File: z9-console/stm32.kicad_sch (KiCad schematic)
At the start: 73 parts, among them J4 Conn_02x20_Odd_Even, J5 ST_STDC14 - SAMTEC_FTSH-107-0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, J7 TC2070 - TAG Connect, SW2 SW_Push, SW3 SW_Push, U3 STM32F427V_G-I_Tx, X2 8MHz 20pF

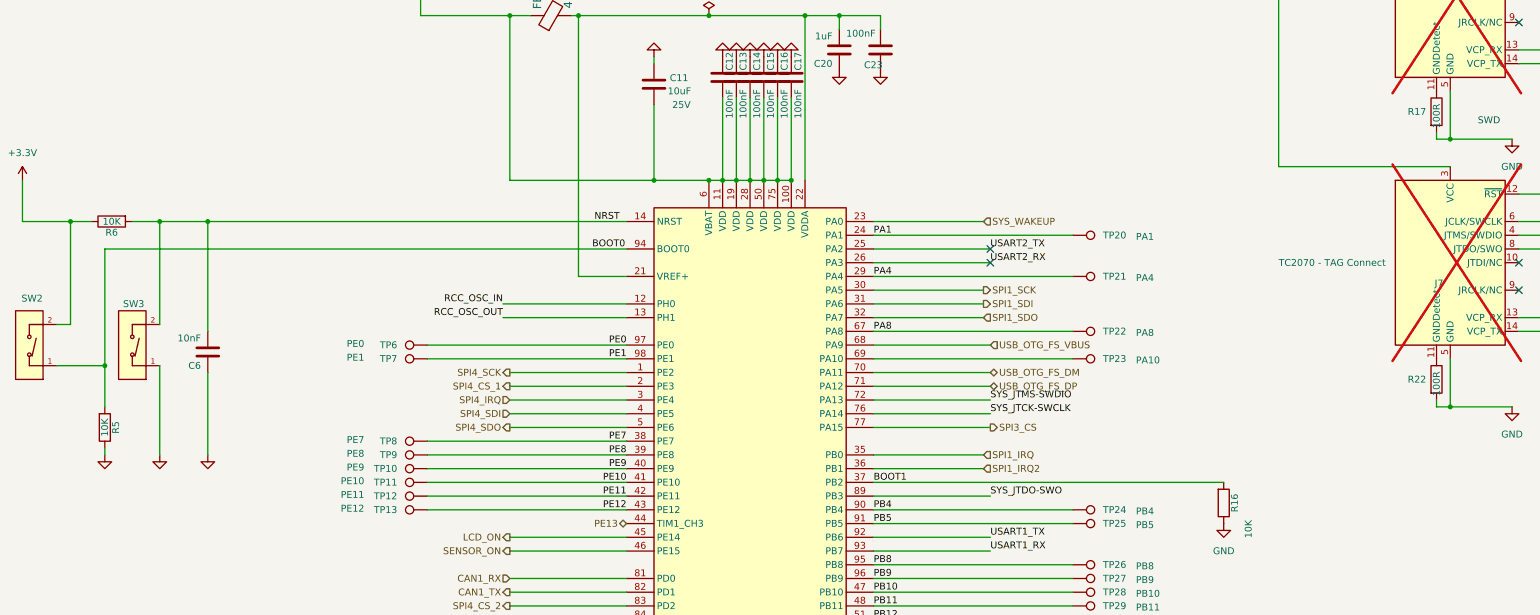
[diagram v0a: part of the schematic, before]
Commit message: lcd power switch-- add new accelerometer
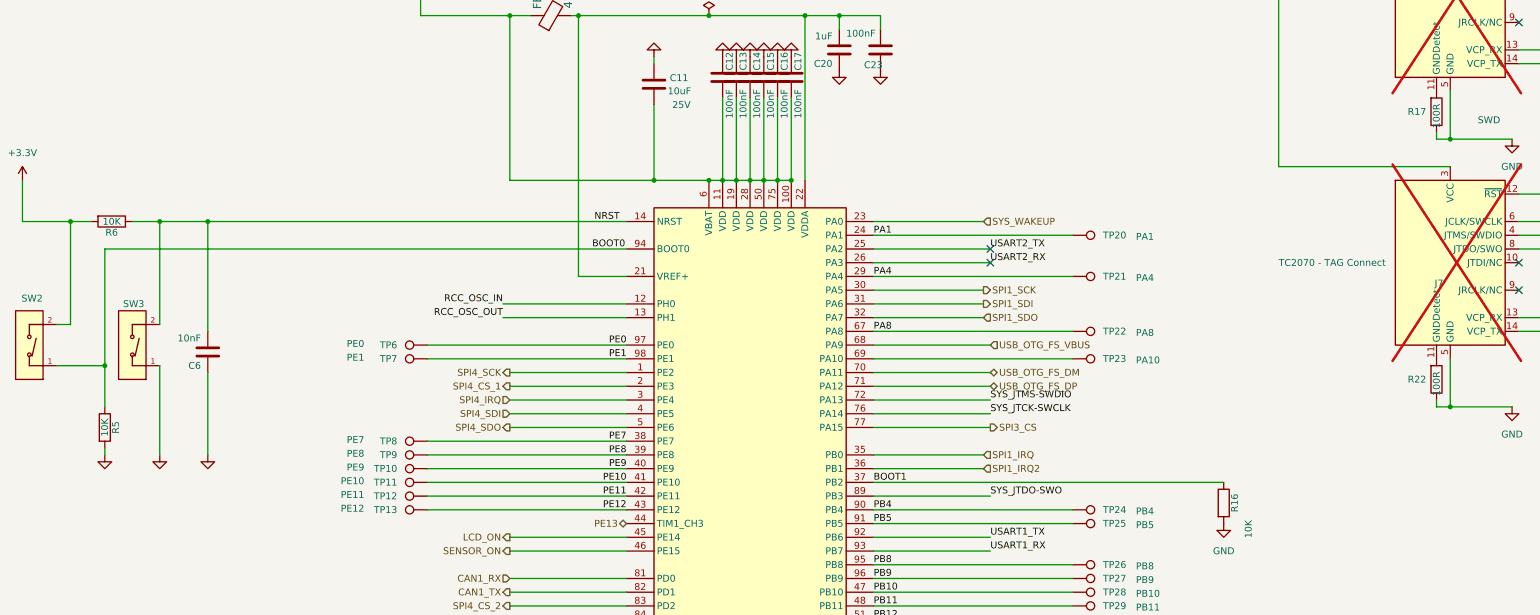
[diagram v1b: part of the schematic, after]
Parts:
- R16, R5, R6: footprint Resistor_SMD:R_0603_1608Metric -> PCM_JLCPCB:R_0402; symbol Device:R -> dnt_global:Resistor_0402,10kΩ; Attrition Qty (none) -> 10; Category (none) -> Resistors,Chip Resistor - Surface Mount; Class (none) -> Basic Component; LCSC C25804 -> C25744; Manufacturer (none) -> UNI-ROYAL(Uniroyal Elec); Minimum Qty (none) -> 20; Operating Temperature Range (none) -> -55°C~+155°C; Overload Voltage (Max) (none) -> 50V; Part (none) -> 0402WGF1002TCE; Power(Watts) (none) -> 62.5mW; Price (none) -> 0.004USD; Process (none) -> SMT; Resistance (none) -> 10kΩ; Stock (none) -> 24372091; Temperature Coefficient (none) -> ±100ppm/°C; Tolerance (none) -> ±1%; Type (none) -> Thick Film Resistors
- R17, R22: footprint Resistor_SMD:R_0603_1608Metric -> PCM_JLCPCB:R_0402; symbol Device:R -> dnt_global:Resistor_0402,10kΩ; Attrition Qty (none) -> 10; Category (none) -> Resistors,Chip Resistor - Surface Mount; Class (none) -> Basic Component; LCSC C22775 -> C25744; Manufacturer (none) -> UNI-ROYAL(Uniroyal Elec); Minimum Qty (none) -> 20; Operating Temperature Range (none) -> -55°C~+155°C; Overload Voltage (Max) (none) -> 50V; Part (none) -> 0402WGF1002TCE; Power(Watts) (none) -> 62.5mW; Price (none) -> 0.004USD; Process (none) -> SMT; Resistance (none) -> 10kΩ; Stock (none) -> 24372091; Temperature Coefficient (none) -> ±100ppm/°C; Tolerance (none) -> ±1%; Type (none) -> Thick Film Resistors

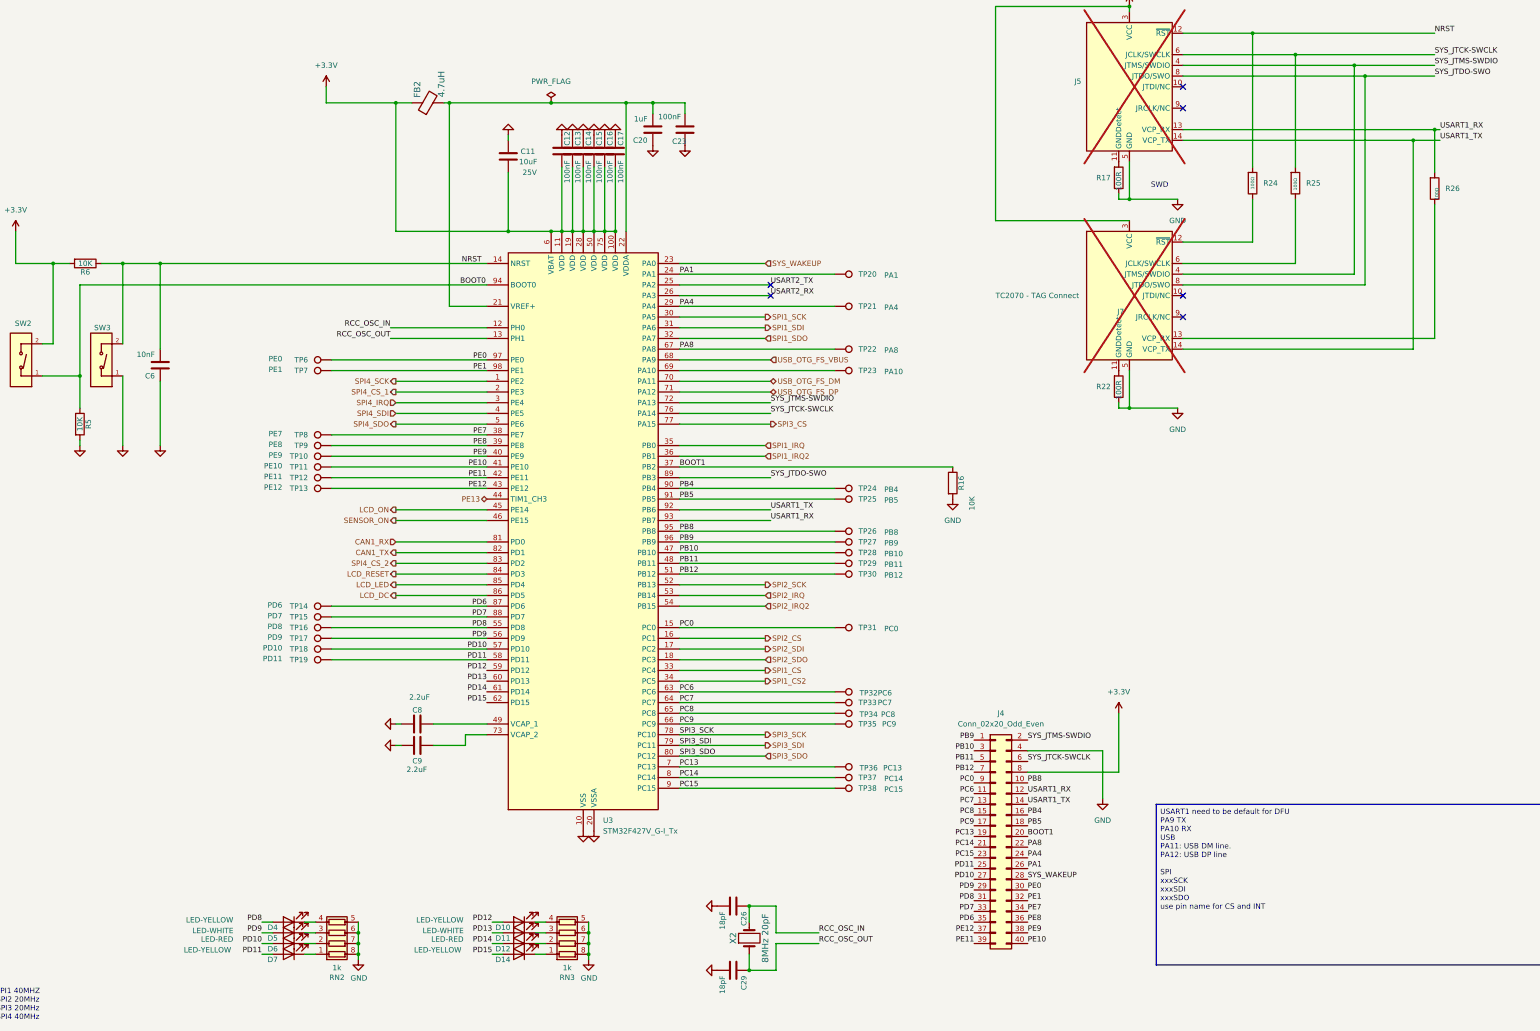
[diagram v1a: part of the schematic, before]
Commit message: change MEMS device
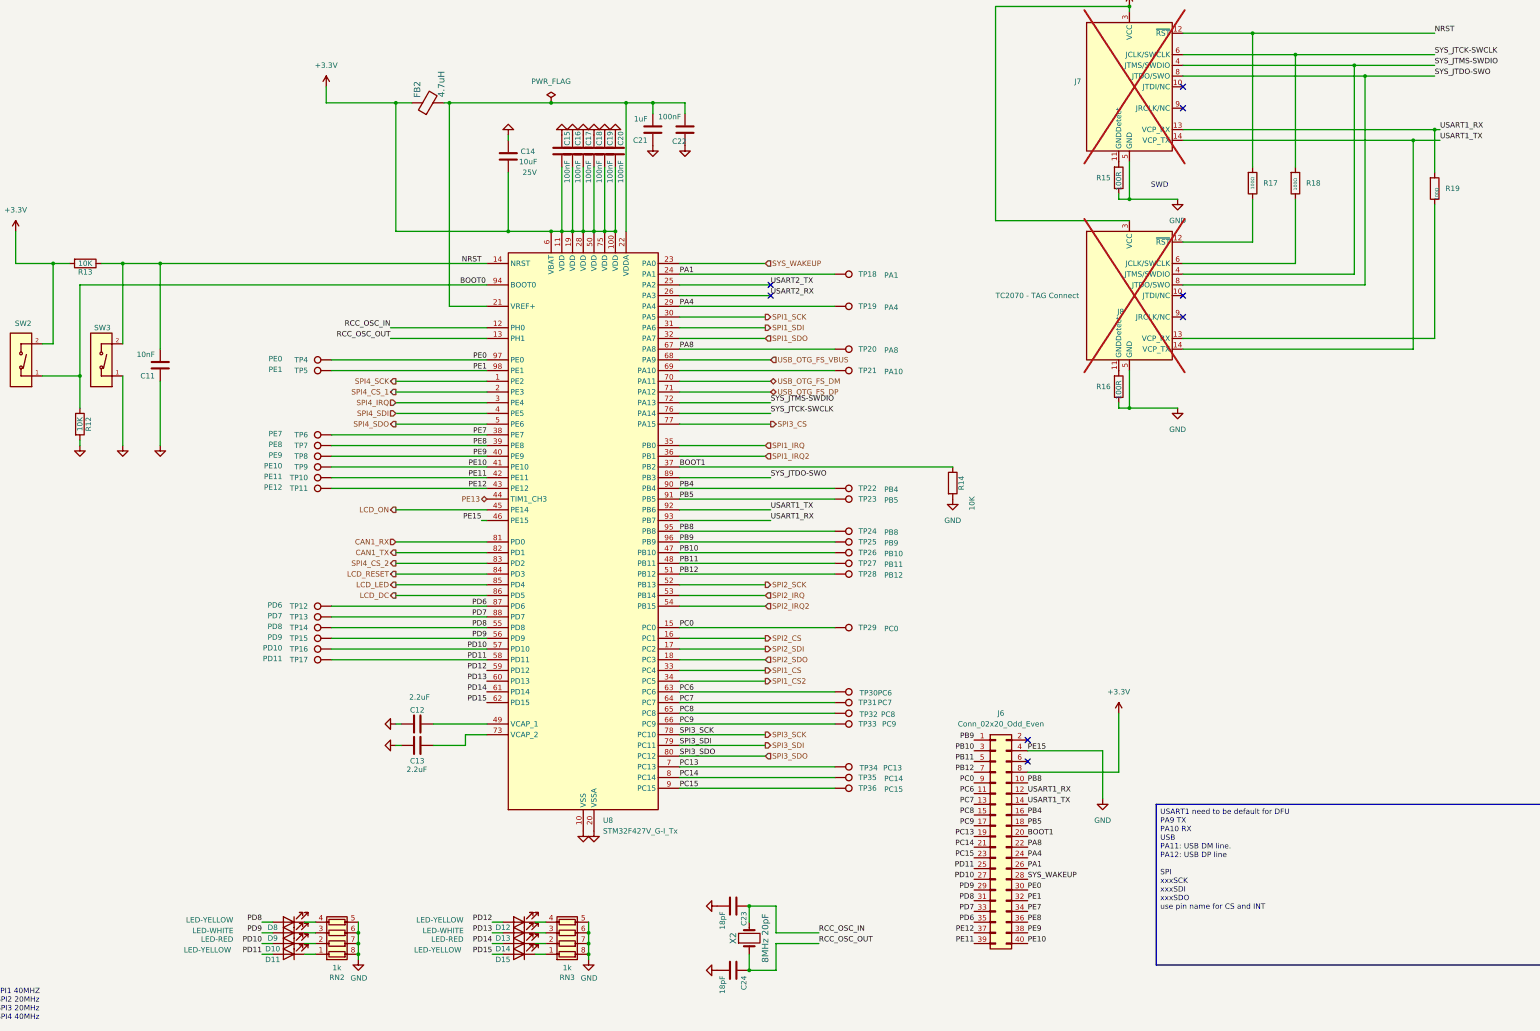
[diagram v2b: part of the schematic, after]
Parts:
- renumbered C6 to C11, C8 to C12, C9 to C13, C11 to C14, C12 to C15, C13 to C16, C14 to C17, C15 to C18, C16 to C19, C17 to C20, C20 to C21, C23 to C22, C26 to C23, C29 to C24, D6 to D10, D7 to D11, D10 to D12, D11 to D13, D12 to D14, D14 to D15, D4 to D8, D5 to D9, J4 to J6, J5 to J7, J7 to J8, R5 to R12, R6 to R13, R16 to R14, R17 to R15, R22 to R16, R24 to R17, R25 to R18, R26 to R19, TP12 to TP10, TP13 to TP11, TP14 to TP12, TP15 to TP13, TP16 to TP14, TP17 to TP15, TP18 to TP16, TP19 to TP17, TP20 to TP18, TP21 to TP19, TP22 to TP20, TP23 to TP21, TP24 to TP22, TP25 to TP23, TP26 to TP24, TP27 to TP25, TP28 to TP26, TP29 to TP27, TP30 to TP28, TP31 to TP29, TP32 to TP30, TP33 to TP31, TP34 to TP32, TP35 to TP33, TP36 to TP34, TP37 to TP35, TP38 to TP36, TP6 to TP4, TP7 to TP5, TP8 to TP6, TP9 to TP7, TP10 to TP8, TP11 to TP9, U3 to U8
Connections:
- net SENSOR_ON is gone; now on net GND: U8.46 (PE15)
- net SYS_JTCK-SWCLK: no longer J6.6 (Pin_6)
- net SYS_JTMS-SWDIO: no longer J6.2 (Pin_2)
- no-connect marks 6 -> 8

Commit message: drc con - fix ti switch reference  - fix stm32  bypass
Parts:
- added C12, C13: 100nF, Capacitor_SMD:C_0603_1608Metric, symbol Device:C
- renumbered C19 to C14, C18 to C15, C12 to C16, C13 to C17, C17 to C18, C16 to C19, C15 to C20, C20 to C21, C14 to C22, C21 to C23, C22 to C24, C23 to C25, C24 to C26, J7 to J6, J8 to J7, J6 to J8
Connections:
- net +3.3V: now also C12.2, C13.2
- net GND: now also C12.1, C13.1
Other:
- moved on the sheet: C11, C14, C15, C16, C17, C18, C19, C20, C21, C22, C23, C24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

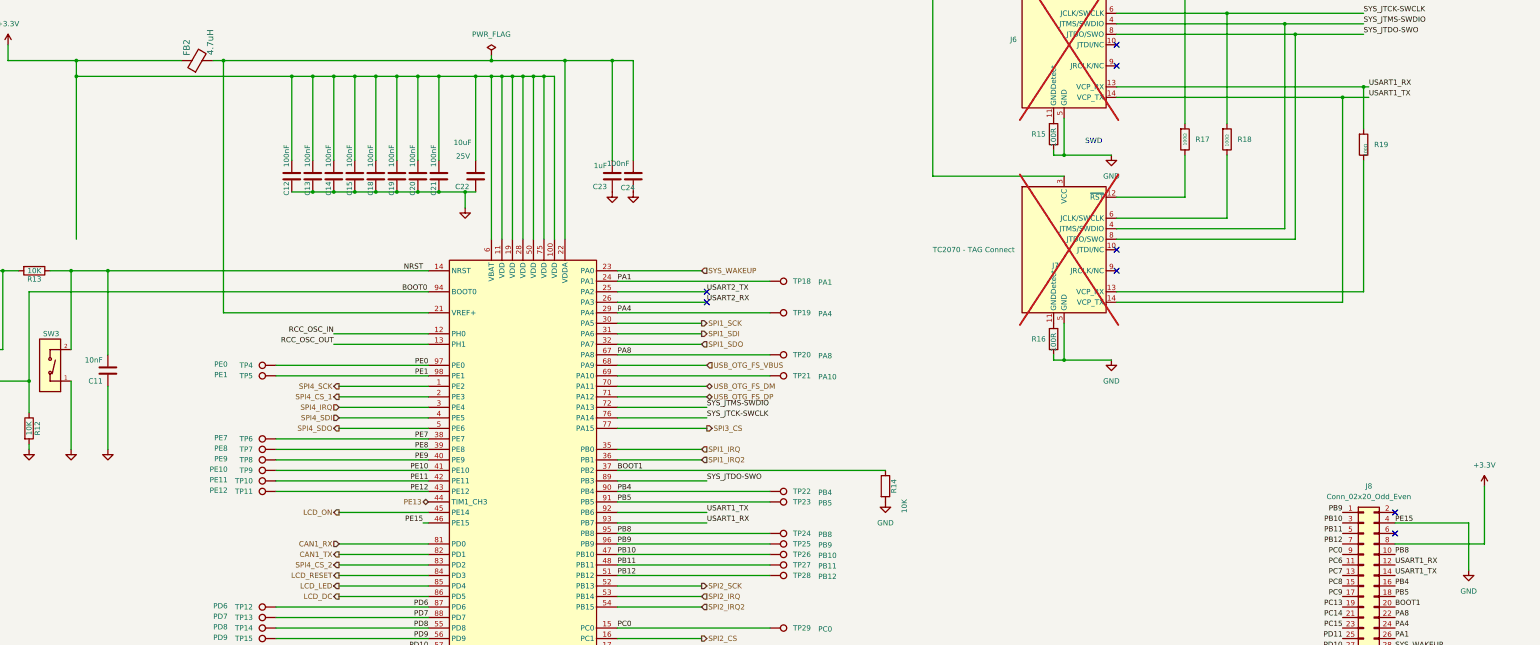
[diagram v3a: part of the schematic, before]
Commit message: drc console complete
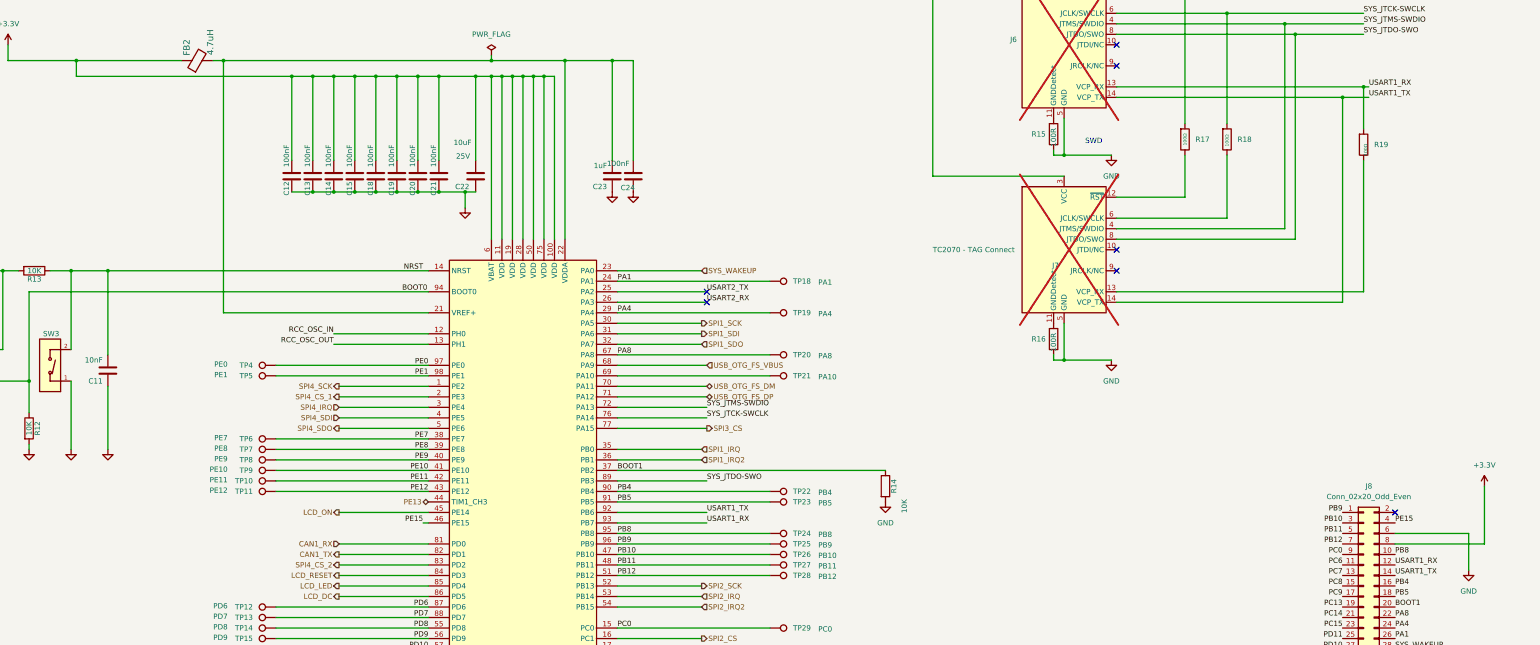
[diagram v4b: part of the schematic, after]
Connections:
- net GND: now also J8.6 (Pin_6); no longer J8.4 (Pin_4), U8.46 (PE15)
- new net PE15: J8.4 (Pin_4), U8.46 (PE15)
- no-connect marks 8 -> 7
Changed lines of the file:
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@@
-	)
-	(junction
-		(at 54.61 60.96)
-		(diameter 0)
-		(color 0 0 0 0)
 	)
 	(junction
@@
 	)
 	(no_connect
-		(at 373.38 171.45)
-	)
-	(no_connect
 		(at 373.38 166.37)
 	)
@@
 	(wire
 		(pts
+			(xy 373.38 171.45) (xy 391.16 171.45)
+		)
+		(stroke
+			(width 0)
+			(type default)
+		)
+	)
+	(wire
+		(pts
 			(xy 62.23 135.89) (xy 62.23 151.13)
 		)
@@
 	(wire
 		(pts
+			(xy 391.16 171.45) (xy 391.16 180.34)
+		)
+		(stroke
+			(width 0)
+			(type default)
+		)
+	)
+	(wire
+		(pts
 			(xy 203.2 247.65) (xy 203.2 251.46)
 		)
@@
 	(wire
 		(pts
-			(xy 54.61 60.96) (xy 54.61 100.33)
-		)
-		(stroke
-			(width 0)
-			(type default)
-		)
-	)
-	(wire
-		(pts
 			(xy 54.61 57.15) (xy 38.1 57.15)
 		)
@@
 	(wire
 		(pts
-			(xy 391.16 168.91) (xy 391.16 180.34)
-		)
-		(stroke
-			(width 0)
-			(type default)
-		)
-	)
-	(wire
-		(pts
 			(xy 87.63 256.54) (xy 90.17 256.54)
 		)
@@
 		)
 		(stroke
-			(width 0)
-			(type default)
-		)
-	)
-	(wire
-		(pts
-			(xy 373.38 168.91) (xy 391.16 168.91)
-		)
-		(stroke

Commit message: final lcsc mappings
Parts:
- removed J8: Conn_02x20_Odd_Even, Connector_PinSocket_2.00mm:PinSocket_2x20_P2.00mm_Vertical_SMD, symbol Connector_Generic:Conn_02x20_Odd_Even
- added TP43: PE15, dnt:TestPoint_Pad_D1.0mm FP .6R, symbol Connector:TestPoint
- C11: footprint Capacitor_SMD:C_0603_1608Metric -> PCM_JLCPCB:C_0402; symbol Device:C -> dnt_global:0402,100nF, 16V; Attrition Qty (none) -> 10; Capacitance (none) -> 100nF; Category (none) -> Capacitors,Multilayer Ceramic Capacitors MLCC - SMD/SMT; Class (none) -> Basic Component; LCSC C57112 -> C1525; Manufacturer (none) -> Samsung Electro-Mechanics; Minimum Qty (none) -> 20; Part (none) -> CL05B104KO5NNNC; Price (none) -> 0.004USD; Process (none) -> SMT; Stock (none) -> 20208285; Temperature Coefficient (none) -> X7R; Tolerance (none) -> ±10%; Voltage Rated (none) -> 16V
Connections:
- net PE15: now also TP43.1
- no-connect marks 7 -> 6
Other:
- moved on the sheet: C12, C13, C14, C15, C18, C19, C20, C21, C22, C23, C24, FB2
